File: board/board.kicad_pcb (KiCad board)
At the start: 2 copper layers, 66.1 x 100.8 mm, 27 parts, among them J1 port attiny, J10 BMS Bat +, J11 BMS Bat gnd, J12 BMS out -, J13 BMS in +5v, J14 BMS in gnd, J15_C189893 BMS led charge ok, J16 Mp3 D1 led marche ok, J17_C189893 Haut parleur, J18_C189893 Batterie + et -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

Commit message: copie ecran pcb + modif positionnement pad
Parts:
- moved J10 1.65 mm to (90.8, 43.9)
- moved J11 1.44 mm to (90.8, 51.1)
- moved J14 1.24 mm to (68.3, 54.4)
- moved J9 0.91 mm to (90.8, 40.6)
- moved J12 0.64 mm to (90.8, 54.4)
- moved J13 0.38 mm to (68.3, 40.6)
- renumbered J17_C189893 to J17, J18_C189893 to J18, J19_C189893 to J19, J21_C189893 to J21, J5_C189893 to J5
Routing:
- net GND: track 135.5 -> 131.8 mm, vias 3 -> 2
- net Net-(J14-Pin_1): track 44.1 -> 46.3 mm
- net Net-(J10-Pin_1): track 34.1 -> 35.0 mm
- net Net-(J7-Pin_1): track 52.9 -> 53.8 mm
- net Net-(J12-Pin_1): track 52.0 -> 51.3 mm
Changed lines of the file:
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@@
 		)
 		(property "Value" "step up in +"
-			(at 0 -2.51 90)
+			(at -3.32 -2.94 90)
 			(layer "F.SilkS")
 			(effects
@@
 		(descr "Through hole straight pin header, 1x02, 2.54mm pitch, single row")
 		(tags "Through hole pin header THT 1x02 2.54mm single row")
-		(property "Reference" "J5_C189893"
+		(property "Reference" "J5"
 			(at 0 -2.38 0)
 			(layer "F.SilkS")
@@
 		(descr "JST GH series connector, BM02B-GHS-TBT (http://www.jst-mfg.com/product/pdf/eng/eGH.pdf), generated with kicad-footprint-generator")
 		(tags "connector JST GH vertical")
-		(property "Reference" "J17_C189893"
+		(property "Reference" "J17"
 			(at 0 -4 180)
 			(layer "F.SilkS")
@@
 		)
 		(property "Value" "step up in -"
-			(at 3.14 4.52 180)
+			(at -3.86 3.02 270)
 			(layer "F.SilkS")
 			(effects
@@
 	(footprint "Connector_PinHeader_2.54mm:PinHeader_1x01_P2.54mm_Vertical"
 		(layer "F.Cu")
-		(at 90.91 52.5)
+		(at 90.805 51.06)
 		(descr "Through hole straight pin header, 1x01, 2.54mm pitch, single row")
 		(tags "Through hole pin header THT 1x01 2.54mm single row")
@@
 		(descr "JST GH series connector, BM02B-GHS-TBT (http://www.jst-mfg.com/product/pdf/eng/eGH.pdf), generated with kicad-footprint-generator")
 		(tags "connector JST GH vertical")
-		(property "Reference" "J18_C189893"
+		(property "Reference" "J18"
 			(at 0 -4 0)
 			(layer "F.SilkS")
@@
 	(footprint "Connector_PinHeader_2.54mm:PinHeader_1x01_P2.54mm_Vertical"
 		(layer "F.Cu")
-		(at 90.97 42.29)
+		(at 90.805 43.93)
 		(descr "Through hole straight pin header, 1x01, 2.54mm pitch, single row")
 		(tags "Through hole pin header THT 1x01 2.54mm single row")
@@
 	(footprint "Connector_PinHeader_2.54mm:PinHeader_1x01_P2.54mm_Vertical"
 		(layer "F.Cu")
-		(at 90.91 54.99)
+		(at 90.805 54.356)
 		(descr "Through hole straight pin header, 1x01, 2.54mm pitch, single row")
 		(tags "Through hole pin header THT 1x01 2.54mm single row")
@@
 	(footprint "Connector_PinHeader_2.54mm:PinHeader_1x01_P2.54mm_Vertical"
 		(layer "F.Cu")
-		(at 69.46 53.85)
+		(at 68.326 54.356)
 		(descr "Through hole straight pin header, 1x01, 2.54mm pitch, single row")
 		(tags "Through hole pin header THT 1x01 2.54mm single row")
@@
 	(footprint "Connector_PinHeader_2.54mm:PinHeader_1x01_P2.54mm_Vertical"
 		(layer "F.Cu")
-		(at 67.945 40.64)
+		(at 68.326 40.64)
 		(descr "Through hole straight pin header, 1x01, 2.54mm pitch, single row")
 		(tags "Through hole pin header THT 1x01 2.54mm single row")
@@
 		(descr "JST GH series connector, BM02B-GHS-TBT (http://www.jst-mfg.com/product/pdf/eng/eGH.pdf), generated with kicad-footprint-generator")
 		(tags "connector JST GH vertical")
-		(property "Reference" "J19_C189893"
+		(property "Reference" "J19"
 			(at 0 -4 0)
 			(layer "F.SilkS")
@@
 		(descr "JST GH series connector, BM02B-GHS-TBT (http://www.jst-mfg.com/product/pdf/eng/eGH.pdf), generated with kicad-footprint-generator")
 		(tags "connector JST GH vertical")
-		(property "Reference" "J21_C189893"
+		(property "Reference" "J21"
 			(at 0 -4 180)
 			(layer "F.SilkS")
@@
 	(footprint "Connector_PinHeader_2.54mm:PinHeader_1x01_P2.54mm_Vertical"
 		(layer "F.Cu")
-		(at 90.97 39.75)
+		(at 90.805 40.64)
 		(descr "Through hole straight pin header, 1x01, 2.54mm pitch, single row")
 		(tags "Through hole pin header THT 1x01 2.54mm single row")
@@
 	)
 	(segment
-		(start 111.48 96.52)
-		(end 111.5 96.5)
-		(width 0.5)
-		(layer "F.Cu")
-		(net 2)
-	)
-	(segment
 		(start 107.95 96.52)
 		(end 107.95 98.05)
@@
 	)
 	(segment
-		(start 107.95 96.52)
-		(end 111.48 96.52)
-		(width 0.5)
-		(layer "F.Cu")
-		(net 2)
-	)
-	(segment
 		(start 92 107.5)
 		(end 92.5 107)
@@
 	)
 	(via
-		(at 111.5 96.5)
+		(at 109.5 70)
 		(size 0.6)
 		(drill 0.3)
@@
 		(net 2)
 	)
-	(via
-		(at 109.5 70)
-		(size 0.6)
-		(drill 0.3)
-		(layers "F.Cu" "B.Cu")
+	(segment
+		(start 109.5 70)
+		(end 109.5 94.97)
+		(width 0.5)
+		(layer "B.Cu")
 		(net 2)
 	)
@@
 	)
 	(segment
-		(start 109.5 82.5)
-		(end 109.5 70)
-		(width 0.5)
-		(layer "B.Cu")
-		(net 2)
-	)
-	(segment
-		(start 111.5 96.5)
-		(end 111.5 84.5)
+		(start 109.5 94.97)
+		(end 107.95 96.52)
 		(width 0.5)
 		(layer "B.Cu")
@@
 	)
 	(segment
-		(start 111.5 84.5)
-		(end 109.5 82.5)
-		(width 0.5)
-		(layer "B.Cu")
-		(net 2)
-	)
-	(segment
 		(start 107.5 61.5)
 		(end 112.625 56.375)
@@
 	)
 	(segment
-		(start 92.271 41.051)
-		(end 90.97 39.75)
+		(start 94.5 41.5)
+		(end 93.64 40.64)
+		(width 0.5)
+		(layer "B.Cu")
+		(net 11)
+	)
+	(segment
+		(start 100 79.5)
+		(end 100 69)
+		(width 0.5)
+		(layer "B.Cu")
+		(net 11)
+	)
+	(segment
+		(start 93.64 40.64)
+		(end 90.805 40.64)
 		(width 0.5)
 		(layer "B.Cu")
@@
 	)
 	(segment
-		(start 92.271 71.771)
-		(end 92.271 41.051)
+		(start 94.5 63.5)
+		(end 94.5 41.5)
 		(width 0.5)
 		(layer "B.Cu")
@@
 	(segment
 		(start 101.5 81)
-		(end 92.271 71.771)
+		(end 100 79.5)
 		(width 0.5)
 		(layer "B.Cu")
@@
 	)
 	(segment
-		(start 114.5 58)
-		(end 114.5 55.5)
+		(start 100 69)
+		(end 94.5 63.5)
 		(width 0.5)
-		(layer "F.Cu")
-		(net 12)
+		(layer "B.Cu")
+		(net 11)
 	)
 	(segment
-		(start 90.91 54.99)
-		(end 92.965 54.99)
+		(start 114.5 58)
+		(end 114.5 55.5)
 		(width 0.5)
 		(layer "F.Cu")
@@
 	)
 	(segment
-		(start 96 51.955)
-		(end 96 51)
+		(start 96 51)
+		(end 92.644 54.356)
 		(width 0.5)
 		(layer "F.Cu")
@@
 	)
 	(segment
-		(start 115.426 58.926)
-		(end 114.5 58)
+		(start 92.644 54.356)
+		(end 90.805 54.356)
 		(width 0.5)
 		(layer "F.Cu")
@@
 	)
 	(segment
-		(start 92.965 54.99)
-		(end 96 51.955)
+		(start 115.426 58.926)
+		(end 114.5 58)
 		(width 0.5)
 		(layer "F.Cu")
@@
 	)
 	(segment
-		(start 108.585 22.86)
-		(end 107.315 24.13)
+		(start 111.76 22.86)
+		(end 108.585 22.86)
+		(width 0.5)
+		(layer "F.Cu")
+		(net 13)
+	)
+	(segment
+		(start 112.45 25.86)
+		(end 112.45 23.55)
 		(width 0.5)
 		(layer "F.Cu")
@@
 	(segment
 		(start 107.315 24.13)
-		(end 107.315 27.305)
+		(end 107.315 27.42)
 		(width 0.5)
 		(layer "F.Cu")
@@
 	)
 	(segment
-		(start 112.45 23.55)
-		(end 111.76 22.86)
+		(start 107.315 27.42)
+		(end 90.805 43.93)
 		(width 0.5)
 		(layer "F.Cu")
@@
 	)
 	(segment
-		(start 107.315 27.305)
-		(end 92.33 42.29)
+		(start 112.45 23.55)
+		(end 111.76 22.86)
 		(width 0.5)
 		(layer "F.Cu")
@@
 	)
 	(segment
-		(start 112.45 25.86)
-		(end 112.45 23.55)
+		(start 108.585 22.86)
+		(end 107.315 24.13)
 		(width 0.5)
 		(layer "F.Cu")
@@
 	)
 	(segment
-		(start 111.76 22.86)
-		(end 108.585 22.86)
+		(start 90.805 49.685)
+		(end 90.805 51.06)
 		(width 0.5)
 		(layer "F.Cu")
-		(net 13)
+		(net 14)
 	)
 	(segment
-		(start 92.33 42.29)
-		(end 90.97 42.29)
+		(start 111.2 32.12)
+		(end 111.06 32.26)
 		(width 0.5)
 		(layer "F.Cu")
-		(net 13)
+		(net 14)
 	)
 	(segment
-		(start 90.91 50.048292)
-		(end 90.91 52.5)
+		(start 111.06 32.26)
+		(end 108.23 32.26)
 		(width 0.5)
 		(layer "F.Cu")
@@
 	(segment
 		(start 111.2 25.86)
-		(end 111.2 29.758292)
+		(end 111.2 32.12)
 		(width 0.5)
 		(layer "F.Cu")
@@
 	)
 	(segment
-		(start 111.2 29.758292)
-		(end 90.91 50.048292)
+		(start 108.23 32.26)
+		(end 90.805 49.685)
 		(width 0.5)
 		(layer "F.Cu")
@@
 	)
 	(segment
-		(start 94.615 28.218636)
-		(end 94.615 24.13)
+		(start 100.89 25.010001)
+		(end 98.739999 22.86)
 		(width 0.5)
 		(layer "F.Cu")
@@
 	)
 	(segment
-		(start 100.89 25.010001)
-		(end 100.89 25.86)
+		(start 95.885 22.86)
+		(end 94.615 24.13)
 		(width 0.5)
 		(layer "F.Cu")
@@
 	)
 	(segment
-		(start 95.885 22.86)
-		(end 98.739999 22.86)
+		(start 94.615 28.218636)
+		(end 82.193636 40.64)
 		(width 0.5)
 		(layer "F.Cu")
@@
 	)
 	(segment
-		(start 98.739999 22.86)
-		(end 100.89 25.010001)
+		(start 94.615 24.13)
+		(end 94.615 28.218636)
 		(width 0.5)
 		(layer "F.Cu")
@@
 	)
 	(segment
-		(start 83.083636 39.75)
-		(end 94.615 28.218636)
+		(start 82.193636 40.64)
+		(end 68.326 40.64)
 		(width 0.5)
 		(layer "F.Cu")
@@
 	)
 	(segment
-		(start 67.945 40.64)
-		(end 68.835 39.75)
+		(start 100.89 25.86)
+		(end 100.89 25.010001)
 		(width 0.5)
 		(layer "F.Cu")
@@
 	)
 	(segment
-		(start 94.615 24.13)
+		(start 98.739999 22.86)
 		(end 95.885 22.86)
 		(width 0.5)
@@
 	)
 	(segment
-		(start 68.835 39.75)
-		(end 83.083636 39.75)
+		(start 69.975 53.85)
+		(end 68.832 53.85)
 		(width 0.5)
 		(layer "F.Cu")
-		(net 15)
+		(net 16)
 	)
 	(segment
@@
 	)
 	(segment
-		(start 69.975 53.85)
-		(end 69.46 53.85)
+		(start 94.805 36.195)
+		(end 87.63 36.195)
 		(width 0.5)
 		(layer "F.Cu")
@@
 	)
 	(segment
-		(start 99.64 29.758292)
-		(end 93.203292 36.195)
+		(start 99.64 31.36)
+		(end 94.805 36.195)
 		(width 0.5)
 		(layer "F.Cu")
@@
 	(segment
 		(start 99.64 25.86)
-		(end 99.64 29.758292)
+		(end 99.64 31.36)
 		(width 0.5)
 		(layer "F.Cu")
@@
 	)
 	(segment
-		(start 93.203292 36.195)
-		(end 87.63 36.195)
+		(start 68.832 53.85)
+		(end 68.326 54.356)
 		(width 0.5)
 		(layer "F.Cu")

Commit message: mise a jour pcb
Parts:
- removed C1, C2: C, Capacitor_THT:CP_Radial_D5.0mm_P2.50mm
- removed J15_C189893: BMS led charge ok, Connector_JST:JST_GH_BM02B-GHS-TBT_1x02-1MP_P1.25mm_Vertical
- removed J16: Mp3 D1 led marche ok, Connector_PinHeader_2.54mm:PinHeader_1x02_P2.54mm_Vertical
- removed J17: Haut parleur, Connector_JST:JST_GH_BM02B-GHS-TBT_1x02-1MP_P1.25mm_Vertical
- removed J18: Batterie + et -, Connector_JST:JST_GH_BM02B-GHS-TBT_1x02-1MP_P1.25mm_Vertical
- removed J19: BMS in + et -, Connector_JST:JST_GH_BM02B-GHS-TBT_1x02-1MP_P1.25mm_Vertical
- removed J20: BMS led charge ok, Connector_PinSocket_2.54mm:PinSocket_1x02_P2.54mm_Vertical
- removed J21: Vers bouton vol - et next, Connector_JST:JST_GH_BM02B-GHS-TBT_1x02-1MP_P1.25mm_Vertical
- removed J22_C189893: Mp3 D1 led marche ok, Connector_JST:JST_GH_BM02B-GHS-TBT_1x02-1MP_P1.25mm_Vertical
- removed J23-C189893: alim +5 gnd, Connector_JST:JST_GH_BM02B-GHS-TBT_1x02-1MP_P1.25mm_Vertical
- added C3: C_C22388053, Capacitor_SMD:CP_Elec_6.3x7.7, F.Cu at (99.1, 108.4)
- added C4: C_C22388053, Capacitor_SMD:CP_Elec_6.3x7.7, F.Cu at (100.6, 50.3)
- added J24: port 3-C265421, Connector_JST:JST_GH_SM12B-GHS-TB_1x12-1MP_P1.25mm_Horizontal, F.Cu at (84.0, 117.3)
- J7: value step up in + -> +
- J8: value step up in - -> -
- R1, R2: value 4.7kΩ _C2907499 -> 4.7kΩ _C17936
- moved J6 36.0 mm to (81.7, 84.2)
- moved J8 34.9 mm to (78.1, 65.9)
- moved J7 28.3 mm to (81.7, 65.9)
- moved J2 5.23 mm to (81.5, 104.2), turned to -90 degrees
- renumbered J5 to J5_C189893
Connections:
- J7 pad 1: Net-(J7-Pin_1) -> Net-(J23-Pin_2)
- J9 pad 1: Net-(J7-Pin_1) -> Net-(J23-Pin_1)
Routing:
- net Net-(J23-Pin_1): track 0.00 -> 80.7 mm
- net Net-(J23-Pin_2): track 0.00 -> 66.5 mm, vias 0 -> 2
- net Net-(J16-Pin_1): track 63.1 -> 0.00 mm, vias 1 -> 0
- net Net-(J16-Pin_2): track 60.0 -> 0.00 mm, vias 1 -> 0
- net Net-(J7-Pin_1): track 53.8 -> 0.00 mm, vias 1 -> 0
- net Net-(J10-Pin_1): track 35.0 -> 85.5 mm, vias 0 -> 4
- net Net-(J11-Pin_1): track 35.3 -> 77.2 mm, vias 0 -> 1
- net Net-(J13-Pin_1): track 44.1 -> 79.6 mm
- net Net-(J1-Pin_4): track 65.4 -> 31.2 mm, vias 2 -> 0
- net Net-(J12-Pin_1): track 51.3 -> 17.4 mm, vias 2 -> 0
- net Net-(J14-Pin_1): track 46.3 -> 71.8 mm
- net VCC: track 166.4 -> 141.0 mm, vias 1 -> 4
- net Net-(J1-Pin_5): track 62.0 -> 38.1 mm
- net Net-(J15_C189893-Pin_2): track 19.8 -> 0.00 mm
- net GND: track 131.8 -> 114.7 mm
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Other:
- board size 66.1 x 100.8 mm -> 44.3 x 82.8 mm
- board text added: "1"
- board text added: "1 : bat + 2 : bat gnd 3 : BMS in + 4 : BMS in gnd 5 : on/off 6 : on/off 7 : HP + 8 : HP - 9 : bouton VOL - 10 : bouton NEXT 11 : vcc 12 : gnd"
- board text added: "12"
- board text added: "8"
- board text removed: "+"
- board text removed: "vcc"

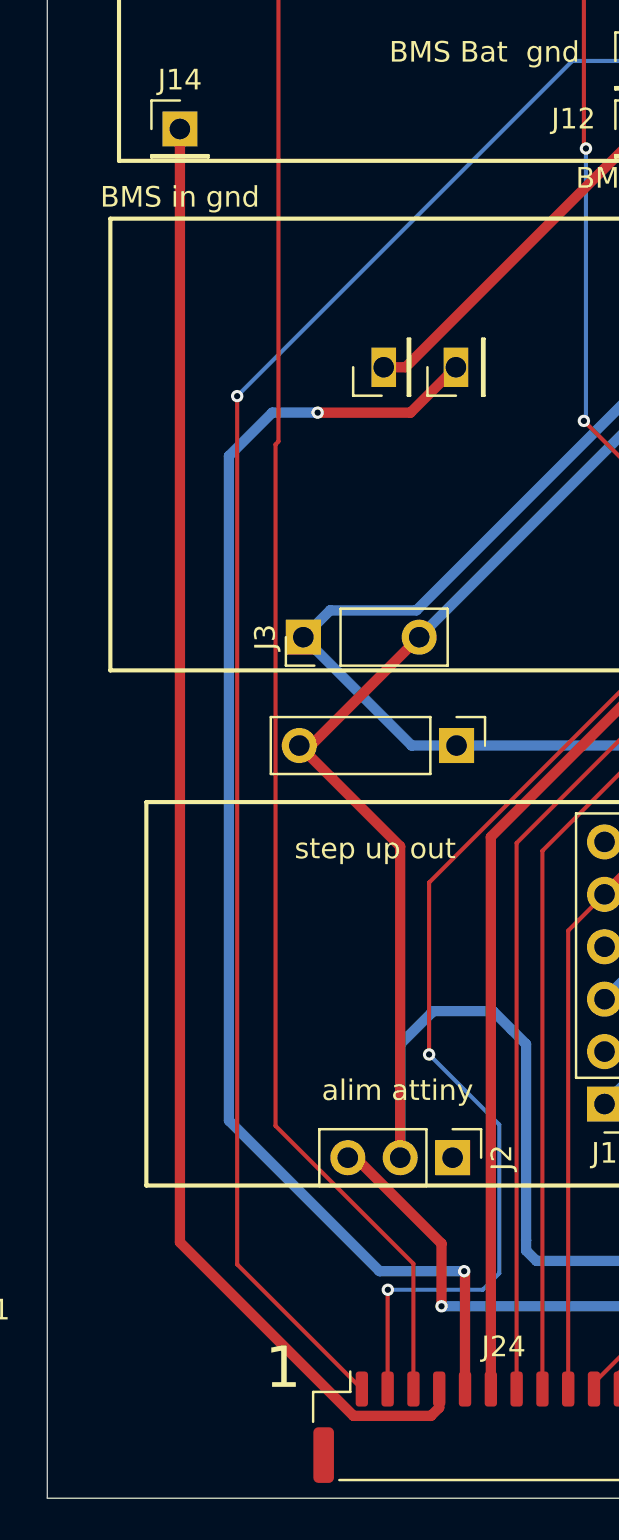
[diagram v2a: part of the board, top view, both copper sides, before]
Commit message: correction pcb , ajout copie d'ecran, et modification readme
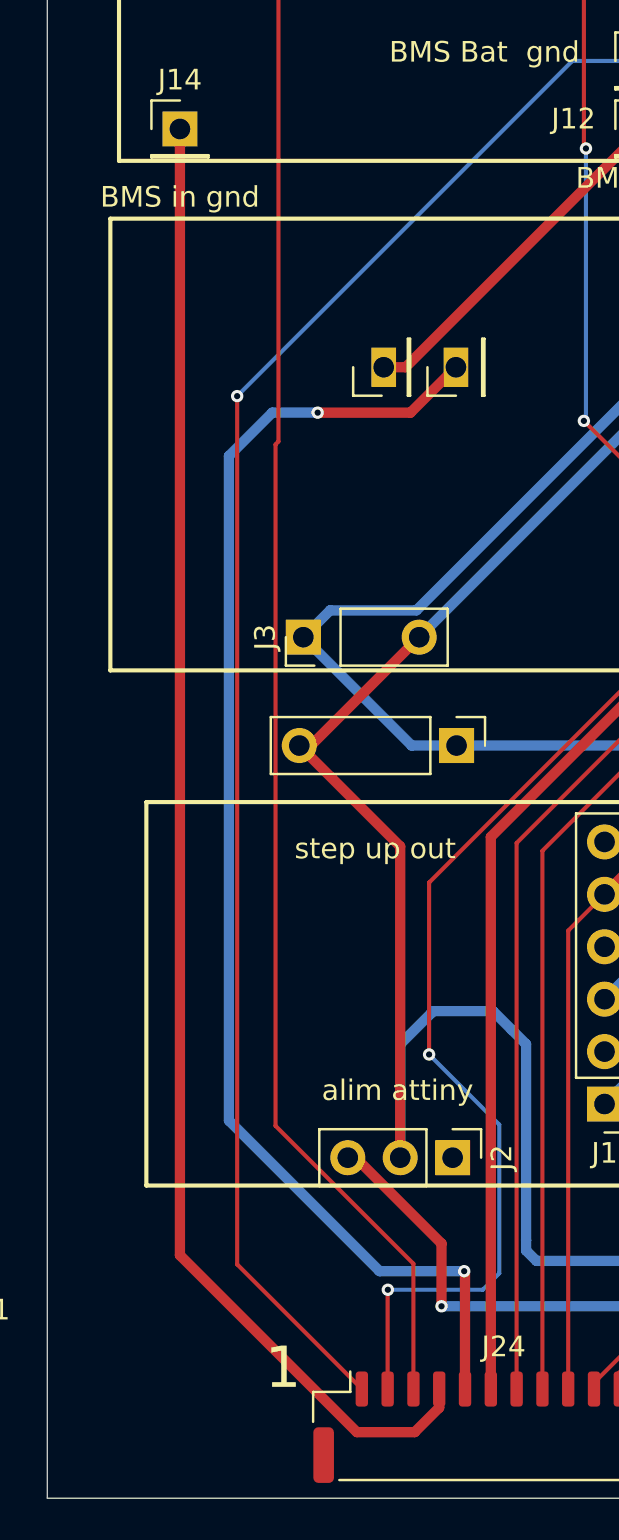
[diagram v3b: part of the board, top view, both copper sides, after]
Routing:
- net Net-(J14-Pin_1): track 71.8 -> 72.8 mm
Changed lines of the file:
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@@
+	)
+	(segment
+		(start 76.9 117.5)
+		(end 79.7 117.5)
+		(width 0.5)
+		(layer "F.Cu")
+		(net 13)
+	)
+	(segment
+		(start 68.326 54.356)
+		(end 68.326 108.926)
+		(width 0.5)
+		(layer "F.Cu")
+		(net 13)
 	)
 	(segment
@@
 	)
 	(segment
-		(start 76.7369 116.711)
-		(end 80.489 116.711)
+		(start 79.7 117.5)
+		(end 80.89 116.31)
 		(width 0.5)
 		(layer "F.Cu")
@@
 	)
 	(segment
-		(start 68.326 54.356)
-		(end 68.326 108.3001)
-		(width 0.5)
-		(layer "F.Cu")
-		(net 13)
-	)
-	(segment
-		(start 68.326 108.3001)
-		(end 76.7369 116.711)
+		(start 68.326 108.926)
+		(end 76.9 117.5)
 		(width 0.5)
 		(layer "F.Cu")
@@
 		(width 0.5)
 		(layer "F.Cu")
-		(net 13)
-	)
-	(segment
-		(start 80.489 116.711)
-		(end 80.89 116.31)
-		(width 0.5)
-		(layer "F.Cu")

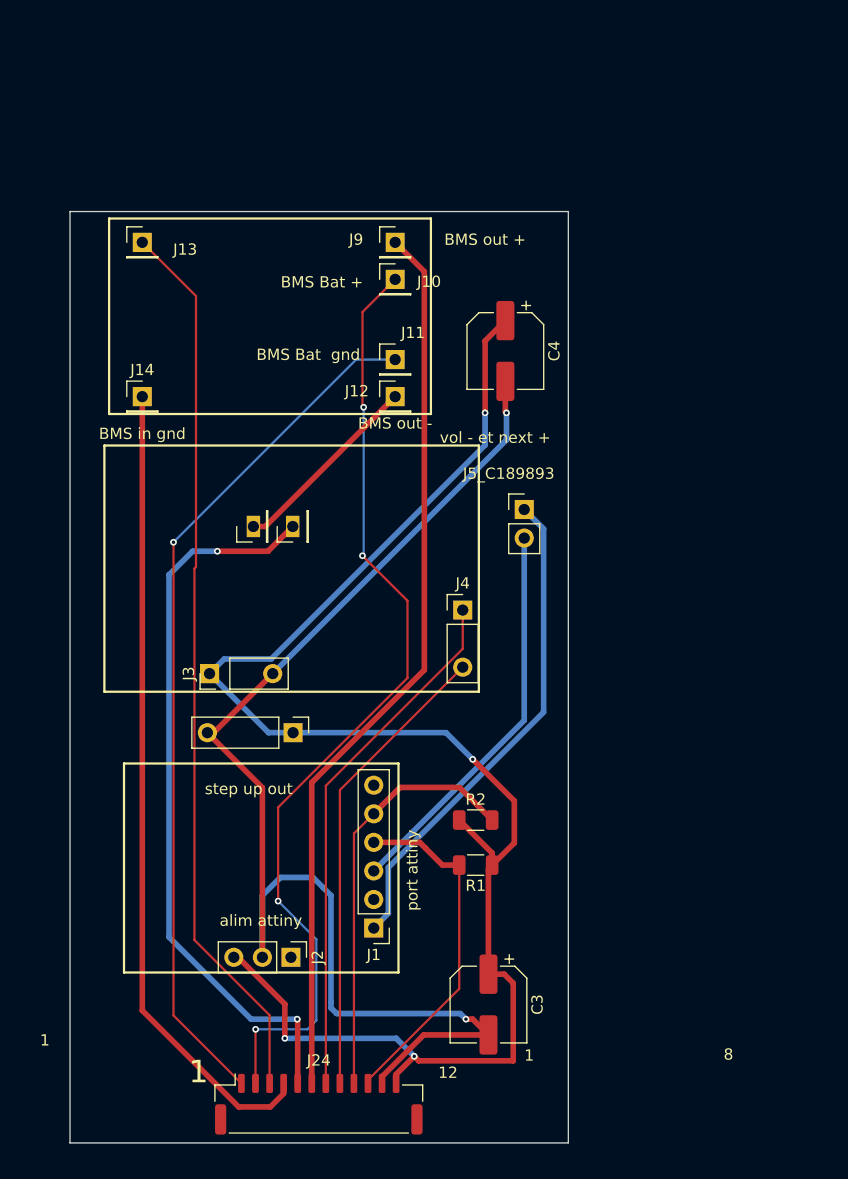
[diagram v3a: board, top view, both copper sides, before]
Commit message: ajout serigraphie pour faciliter le montage
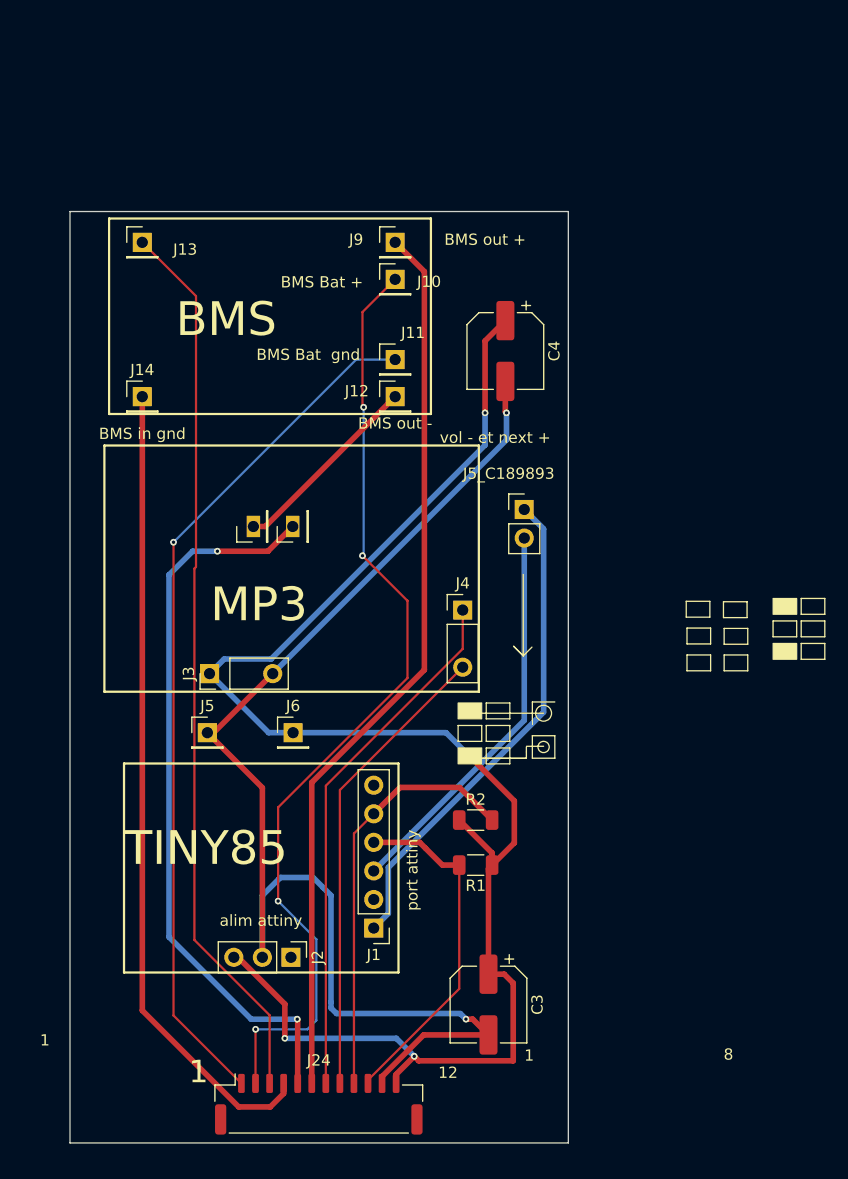
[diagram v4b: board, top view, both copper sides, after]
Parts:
- added J5: step up in +, Connector_PinHeader_2.54mm:PinHeader_1x01_P2.54mm_Vertical, F.Cu at (74.1, 84.2)
- J6: value step up out -> step up in +; footprint Library:PinHeader_1x04_P2.54mm_Vertical-mp3 -> Connector_PinHeader_2.54mm:PinHeader_1x01_P2.54mm_Vertical
- J7: value + -> step up in +
- J8: value - -> step up in -
- turned J6 to 0 degrees
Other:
- board text added: "BMS"
- board text added: "MP3"
- board text added: "TINY85"
